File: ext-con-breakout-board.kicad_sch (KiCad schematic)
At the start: 9 parts, among them J1 Conn_02x12_Odd_Even, J2 Conn_01x16

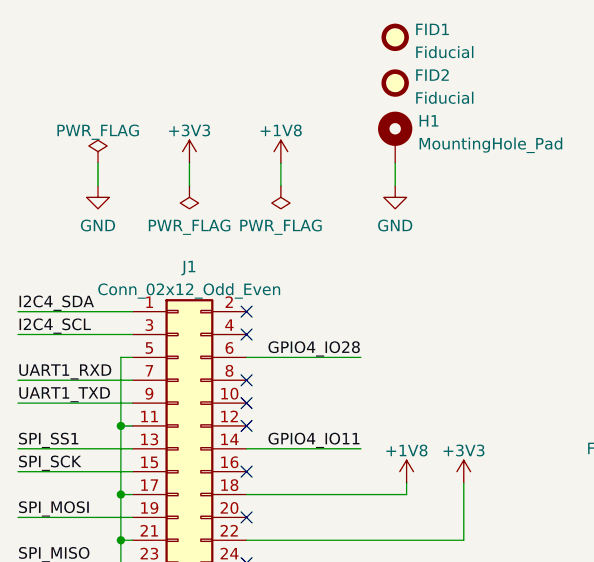
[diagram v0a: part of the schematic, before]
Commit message: Add teardrops to the 0402 pads, add GND trace from C2 to the through hole pin, make the FPC connector part number be Panasonic AXT624124, add a 3D model for the FPC connector, fix and wave all DRCs on KiCad version 7.0.1, and update the board to be v0.7
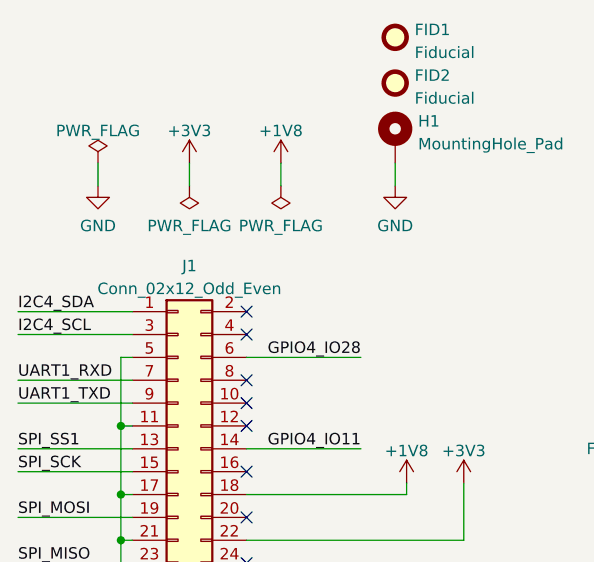
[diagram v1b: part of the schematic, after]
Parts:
- J1: footprint ext-con-breakout-board:OK-06M024-04 -> ext-con-breakout-board:AXT624124; Distrib Link https://www.yoycart.com/Product/528429082566/ -> https://www.digikey.com/en/products/detail/panasonic-electr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; MFG Name OK -> Panasonic; MFG Part Num OK-06M024-04 -> AXT624124; Others https://www.alibaba.com/trade/search?fsb=y&IndexArea=produc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 -> https://octopart.com/search?q=AXT624124&currency=USD&specs=0
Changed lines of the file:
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@@
   )
   (symbol (lib_id "Connector_Generic:Conn_02x12_Odd_Even") (at 110.49 96.52 0) (unit 1)
-    (in_bom yes) (on_board yes) (dnp no) (fields_autoplaced)
-    (property "Reference" "J1" (at 111.76 78.8502 0)
+    (in_bom yes) (on_board yes) (dnp no)
+    (property "Reference" "J1" (at 111.76 78.74 0)
       (effects (font (size 1.27 1.27)))
     )
-    (property "Value" "Conn_02x12_Odd_Even" (at 111.76 81.3871 0)
+    (property "Value" "Conn_02x12_Odd_Even" (at 111.76 81.28 0)
       (effects (font (size 1.27 1.27)))
     )
-    (property "Footprint" "ext-con-breakout-board:OK-06M024-04" (at 110.49 96.52 0)
+    (property "Footprint" "ext-con-breakout-board:AXT624124" (at 110.49 96.52 0)
       (effects (font (size 1.27 1.27)) hide)
     )
-    (property "Datasheet" "https://cloud.puri.sm/s/fnAS9D5KiDy9wMA" (at 110.49 96.52 0)
+    (property "Datasheet" "~" (at 110.49 96.52 0)
       (effects (font (size 1.27 1.27)) hide)
     )
-    (property "MFG Name" "OK" (at 110.49 96.52 0)
+    (property "MFG Name" "Panasonic" (at 110.49 96.52 0)
       (effects (font (size 1.27 1.27)) hide)
     )
-    (property "MFG Part Num" "OK-06M024-04" (at 110.49 96.52 0)
+    (property "MFG Part Num" "AXT624124" (at 110.49 96.52 0)
       (effects (font (size 1.27 1.27)) hide)
     )
-    (property "Distrib Link" "https://www.yoycart.com/Product/528429082566/" (at 110.49 96.52 0)
+    (property "Distrib Link" "https://www.digikey.com/en/products/detail/panasonic-electric-works/AXT624124/1986596" (at 110.49 96.52 0)
       (effects (font (size 1.27 1.27)) hide)
     )
@@
       (effects (font (size 1.27 1.27)) hide)
     )
-    (property "Others" "https://www.alibaba.com/trade/search?fsb=y&IndexArea=product_en&CatId=&tab=all&SearchText=OK-06M024-04" (at 110.49 96.52 0)
+    (property "Others" "https://octopart.com/search?q=AXT624124&currency=USD&specs=0" (at 110.49 96.52 0)
       (effects (font (size 1.27 1.27)) hide)
     )

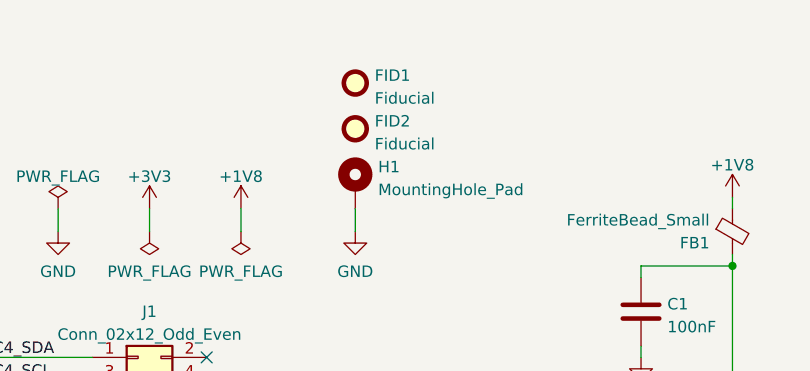
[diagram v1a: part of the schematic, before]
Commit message: Add a silkscreen arrow pointing at the MISO pin
Add a third fiducial. Reduce the thermal relief gap to 0.428mm so that
the GND pins can have four spokes connecting to the copper pour on
ln2.Cu.

Fix the hatched lines drawn in the "Flex Section" on the User.Comments
layer.
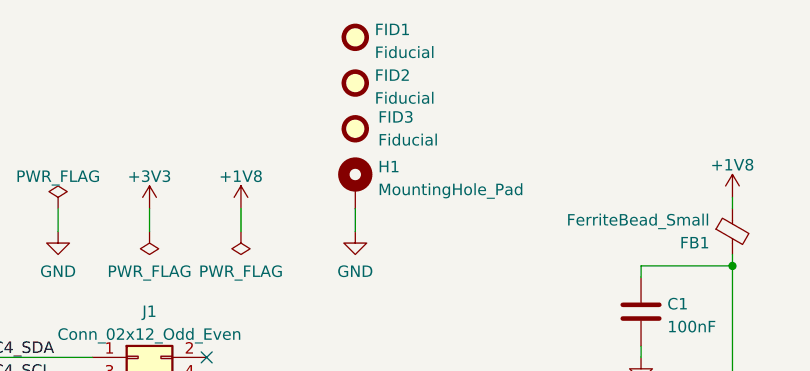
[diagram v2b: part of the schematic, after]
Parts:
- added FID3: Fiducial, ext-con-breakout-board:Fiducial_0.5mm_Mask1mm, symbol Mechanical:Fiducial
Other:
- moved on the sheet: FID1, FID2
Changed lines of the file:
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@@
     )
   )
-  (symbol (lib_id "Mechanical:Fiducial") (at 134.62 53.34 0) (unit 1)
+  (symbol (lib_id "Mechanical:Fiducial") (at 134.62 48.26 0) (unit 1)
     (in_bom yes) (on_board yes) (dnp no) (fields_autoplaced)
-    (property "Reference" "FID1" (at 136.779 52.5053 0)
+    (property "Reference" "FID1" (at 136.779 47.4253 0)
       (effects (font (size 1.27 1.27)) (justify left))
     )
-    (property "Value" "Fiducial" (at 136.779 55.0422 0)
+    (property "Value" "Fiducial" (at 136.779 49.9622 0)
       (effects (font (size 1.27 1.27)) (justify left))
     )
-    (property "Footprint" "ext-con-breakout-board:Fiducial_0.5mm_Mask1mm" (at 134.62 53.34 0)
+    (property "Footprint" "ext-con-breakout-board:Fiducial_0.5mm_Mask1mm" (at 134.62 48.26 0)
       (effects (font (size 1.27 1.27)) hide)
     )
-    (property "Datasheet" "~" (at 134.62 53.34 0)
+    (property "Datasheet" "~" (at 134.62 48.26 0)
       (effects (font (size 1.27 1.27)) hide)
     )
@@
     )
   )
+  (symbol (lib_id "Mechanical:Fiducial") (at 134.62 58.42 0) (unit 1)
+    (in_bom yes) (on_board yes) (dnp no) (fields_autoplaced)
+    (property "Reference" "FID3" (at 137.16 57.15 0)
+      (effects (font (size 1.27 1.27)) (justify left))
+    )
+    (property "Value" "Fiducial" (at 137.16 59.69 0)
+      (effects (font (size 1.27 1.27)) (justify left))
+    )
+    (property "Footprint" "ext-con-breakout-board:Fiducial_0.5mm_Mask1mm" (at 134.62 58.42 0)
+      (effects (font (size 1.27 1.27)) hide)
+    )
+    (property "Datasheet" "~" (at 134.62 58.42 0)
+      (effects (font (size 1.27 1.27)) hide)
+    )
+    (instances
+      (project "ext-con-breakout-board"
+        (path "/298f36e8-6719-4ffe-ac8c-ce72aafb38a0"
+          (reference "FID3") (unit 1)
+        )
+      )
+    )
+  )
   (symbol (lib_id "power:+1V8") (at 176.53 66.04 0) (unit 1)
     (in_bom yes) (on_board yes) (dnp no) (fields_autoplaced)
@@
     )
   )
-  (symbol (lib_id "Mechanical:Fiducial") (at 134.62 58.42 0) (unit 1)
+  (symbol (lib_id "Mechanical:Fiducial") (at 134.62 53.34 0) (unit 1)
     (in_bom yes) (on_board yes) (dnp no) (fields_autoplaced)
-    (property "Reference" "FID2" (at 136.779 57.5853 0)
+    (property "Reference" "FID2" (at 136.779 52.5053 0)
       (effects (font (size 1.27 1.27)) (justify left))
     )
-    (property "Value" "Fiducial" (at 136.779 60.1222 0)
+    (property "Value" "Fiducial" (at 136.779 55.0422 0)
       (effects (font (size 1.27 1.27)) (justify left))
     )
-    (property "Footprint" "ext-con-breakout-board:Fiducial_0.5mm_Mask1mm" (at 134.62 58.42 0)
+    (property "Footprint" "ext-con-breakout-board:Fiducial_0.5mm_Mask1mm" (at 134.62 53.34 0)
       (effects (font (size 1.27 1.27)) hide)
     )
-    (property "Datasheet" "~" (at 134.62 58.42 0)
+    (property "Datasheet" "~" (at 134.62 53.34 0)
       (effects (font (size 1.27 1.27)) hide)
     )
